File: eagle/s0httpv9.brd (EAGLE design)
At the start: 32 parts, among them X1 MKDSN1,5/6-5,08, X2 MKDSN1,5/6-5,08

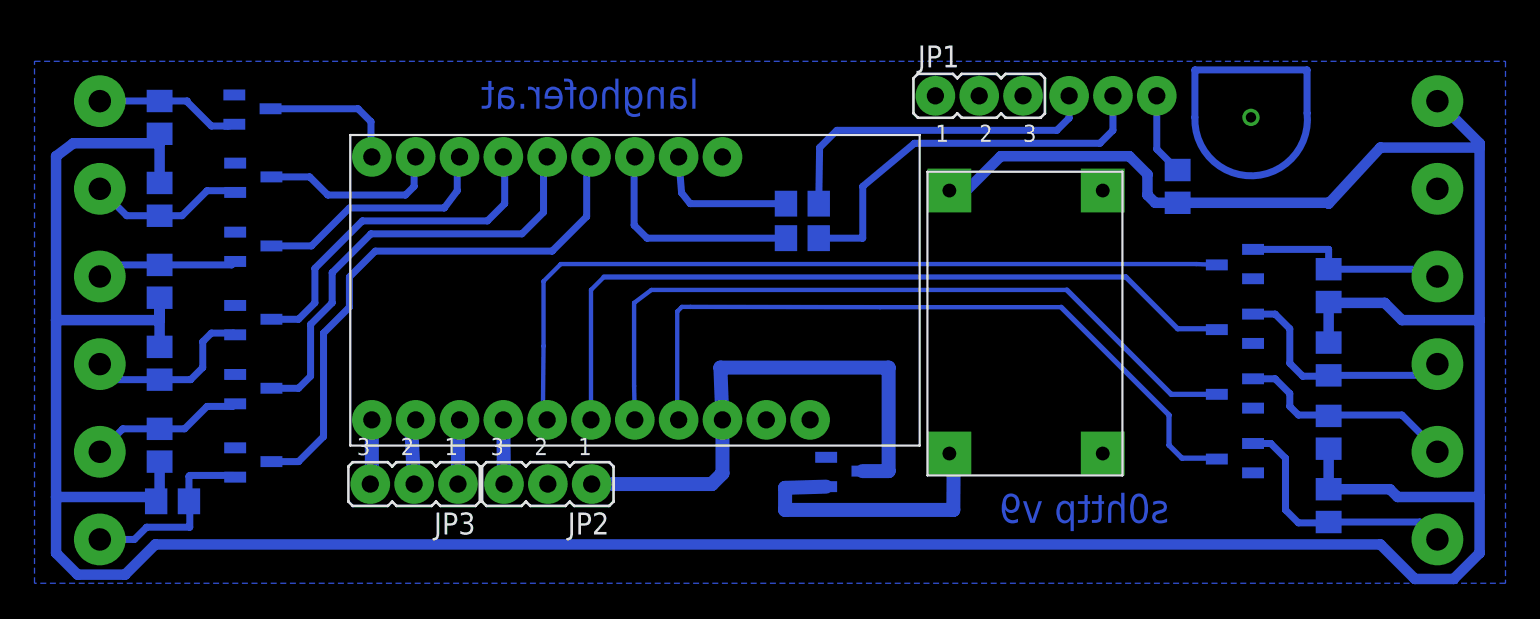
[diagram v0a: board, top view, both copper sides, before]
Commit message: changed to 0.6 thicknes for most connections
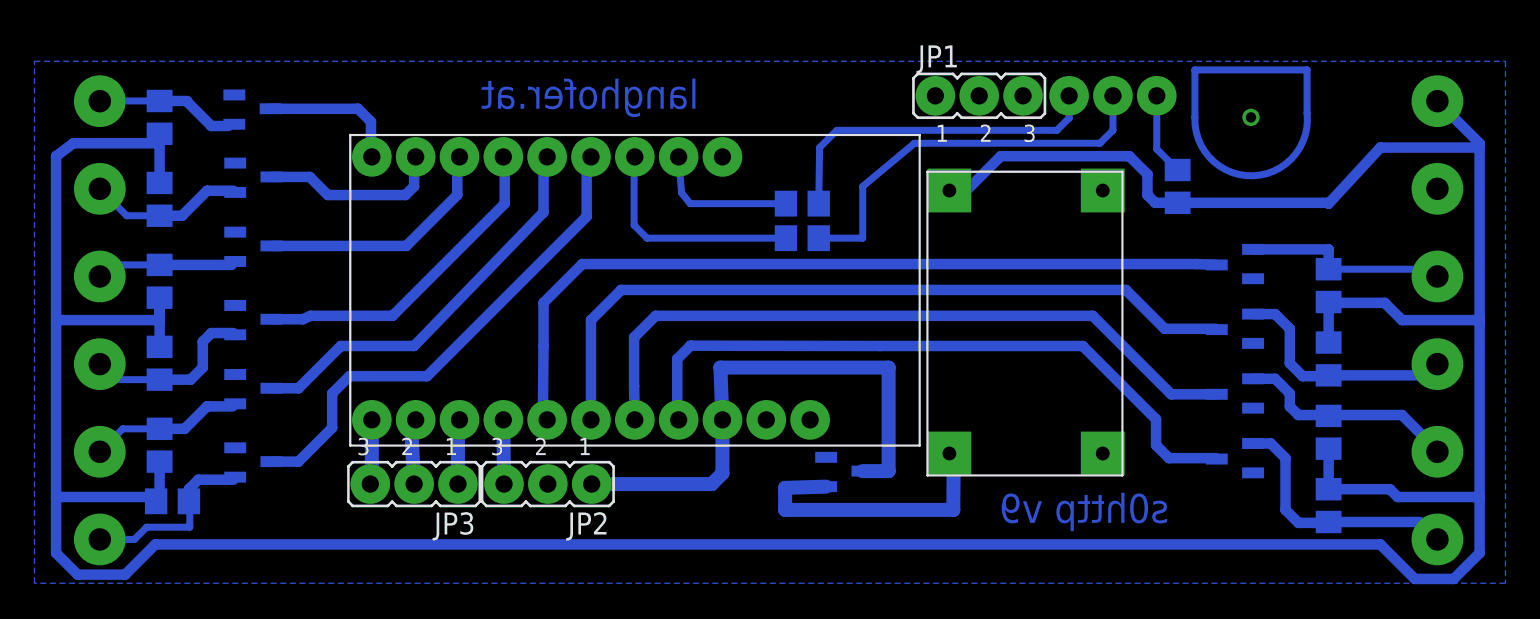
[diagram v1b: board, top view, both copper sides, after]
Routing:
- net N$13: track 43.7 -> 40.1 mm
- net N$17: track 32.4 -> 29.0 mm
- net N$15: track 26.2 -> 23.5 mm
- net N$16: track 43.3 -> 41.0 mm
- net N$24: track 45.4 -> 43.7 mm
- net N$14: track 20.4 -> 19.2 mm
- net N$21: track 47.7 -> 47.0 mm
- net N$28: track 11.2 -> 10.7 mm
